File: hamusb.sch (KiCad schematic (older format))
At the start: 20 parts, among them P1 USB, P2 DATA, Q1 2N7002E, U1 FT232RL, U2 74AC125, Y1 12MHz

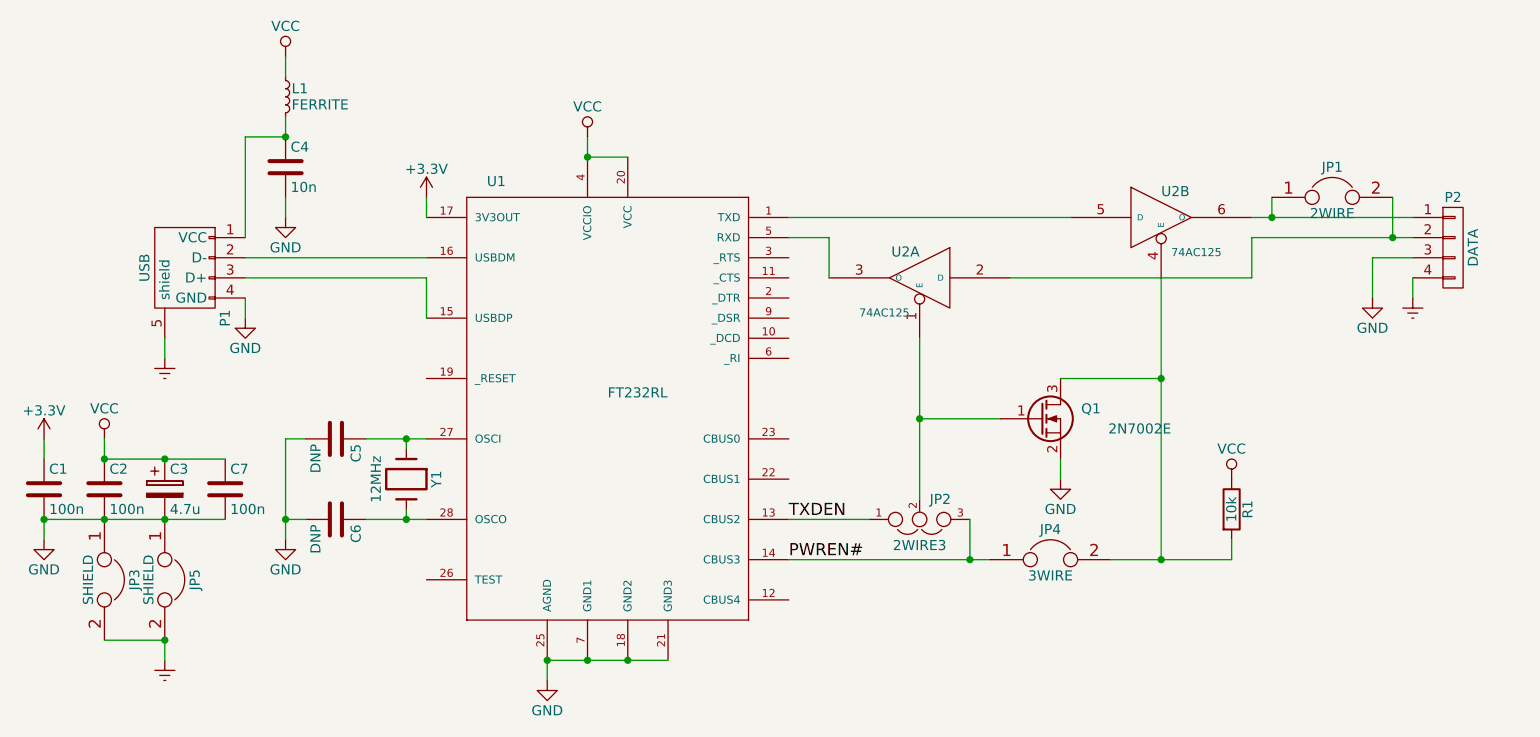
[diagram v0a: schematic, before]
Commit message: Cleanup, swapped logic gates, reordered input power circuit
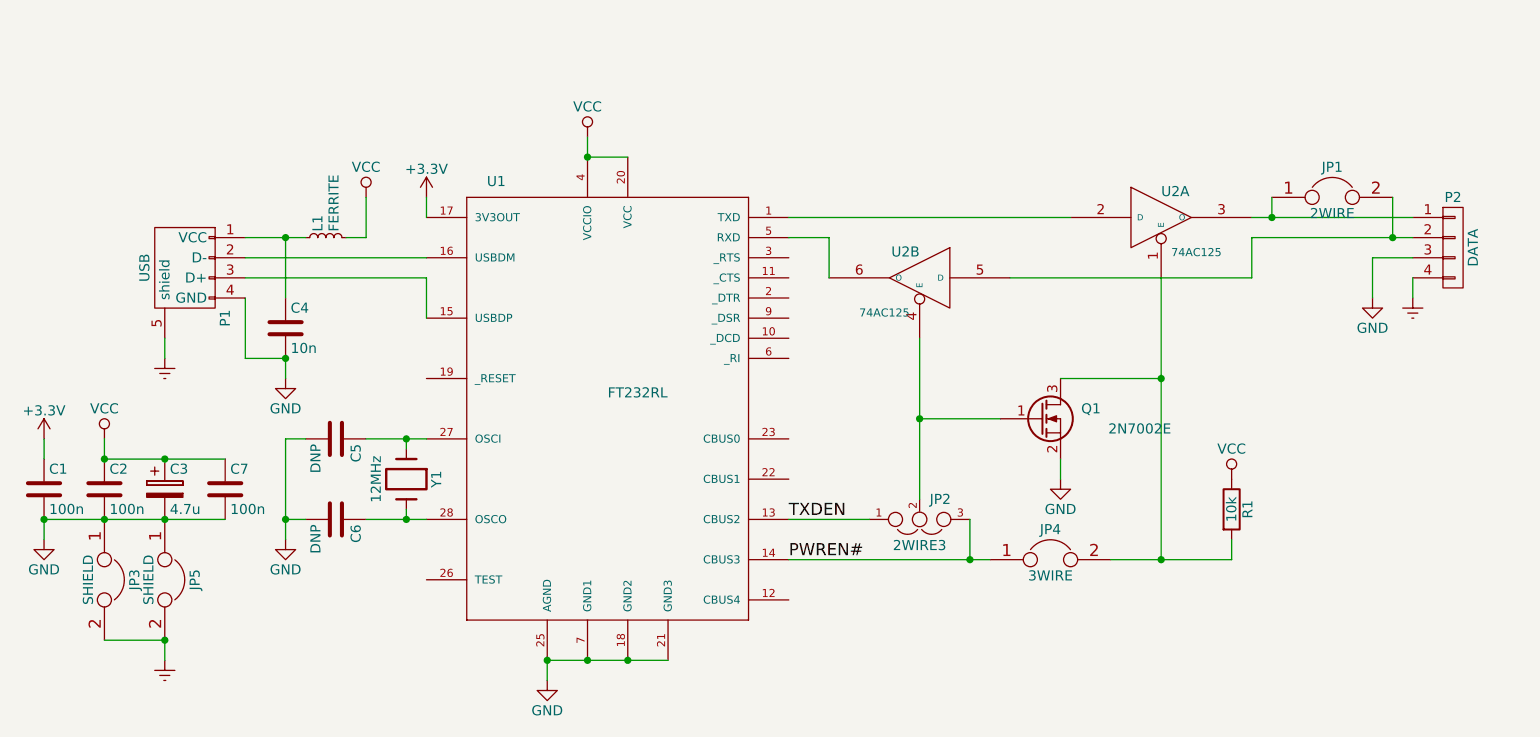
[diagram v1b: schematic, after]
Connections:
- net VCC: now also L1.2; no longer L1.1
- net at U1.1 (TXD): now also U2.2 (D); no longer U2.5 (D)
- net at U1.5 (RXD): now also U2.6 (O); no longer U2.3 (O)
- net at C4.1, P1.1 (VCC): now also L1.1; no longer L1.2
- net at JP1.1, P2.1 (P1): now also U2.3 (O); no longer U2.6 (O)
- net at JP1.2, P2.2 (P2): now also U2.5 (D); no longer U2.2 (D)
- net at JP4.2, Q1.3 (D), R1.2: now also U2.1 (E); no longer U2.4 (E)
- net at JP2.2, Q1.1 (G): now also U2.4 (E); no longer U2.1 (E)
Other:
- moved on the sheet: C4, L1
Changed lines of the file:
@@
 Sheet 1 1
 Title "Ham Radio USB Data Programmer"
-Date "2015-10-26"
-Rev "3"
+Date "2015-10-27"
+Rev "4"
 Comp "© 2015 Gregor Riepl"
 Comment1 "Licensed under the CERN OHL v1.2"
@@
 L C C4
 U 1 1 561BE2FB
-P 3900 2600
-F 0 "C4" H 3925 2700 50  0000 L CNN
-F 1 "10n" H 3925 2500 50  0000 L CNN
-F 2 "Capacitors_SMD:C_0805_HandSoldering" H 3938 2450 30  0001 C CNN
-F 3 "" H 3900 2600 60  0000 C CNN
-	1    3900 2600
+P 3900 3400
+F 0 "C4" H 3925 3500 50  0000 L CNN
+F 1 "10n" H 3925 3300 50  0000 L CNN
+F 2 "Capacitors_SMD:C_0805_HandSoldering" H 3938 3250 30  0001 C CNN
+F 3 "" H 3900 3400 60  0000 C CNN
+	1    3900 3400
 	1    0    0    -1
 $EndComp
@@
 L L_Small L1
 U 1 1 561BE3F0
-P 3900 2250
-F 0 "L1" H 3930 2290 50  0000 L CNN
-F 1 "FERRITE" H 3930 2210 50  0000 L CNN
-F 2 "Resistors_SMD:R_0805_HandSoldering" H 3900 2250 60  0001 C CNN
-F 3 "" H 3900 2250 60  0000 C CNN
-	1    3900 2250
-	1    0    0    -1
+P 4100 2950
+F 0 "L1" H 4130 2990 50  0000 L CNN
+F 1 "FERRITE" H 4130 2910 50  0000 L CNN
+F 2 "Resistors_SMD:R_0805_HandSoldering" H 4100 2950 60  0001 C CNN
+F 3 "" H 4100 2950 60  0000 C CNN
+	1    4100 2950
+	0    -1   -1   0
 $EndComp
 $Comp
@@
 L VCC #PWR07
 U 1 1 561BED9C
-P 3900 2050
-F 0 "#PWR07" H 3900 1900 50  0001 C CNN
-F 1 "VCC" H 3900 2200 50  0000 C CNN
-F 2 "" H 3900 2050 60  0000 C CNN
-F 3 "" H 3900 2050 60  0000 C CNN
-	1    3900 2050
-	1    0    0    -1
-$EndComp
-$Comp
-L GND #PWR08
-U 1 1 561BEE77
-P 3700 3350
-F 0 "#PWR08" H 3700 3100 50  0001 C CNN
-F 1 "GND" H 3700 3200 50  0000 C CNN
-F 2 "" H 3700 3350 60  0000 C CNN
-F 3 "" H 3700 3350 60  0000 C CNN
-	1    3700 3350
-	1    0    0    -1
-$EndComp
-Wire Wire Line
-	3700 3250 3700 3350
-$Comp
-L Earth #PWR09
+P 4300 2750
+F 0 "#PWR07" H 4300 2600 50  0001 C CNN
+F 1 "VCC" H 4300 2900 50  0000 C CNN
+F 2 "" H 4300 2750 60  0000 C CNN
+F 3 "" H 4300 2750 60  0000 C CNN
+	1    4300 2750
+	1    0    0    -1
+$EndComp
+Wire Wire Line
+	3700 3250 3700 3550
+$Comp
+L Earth #PWR08
 U 1 1 561BEEB0
 P 3300 3550
-F 0 "#PWR09" H 3300 3300 50  0001 C CNN
+F 0 "#PWR08" H 3300 3300 50  0001 C CNN
 F 1 "Earth" H 3300 3400 50  0001 C CNN
 F 2 "" H 3300 3550 60  0000 C CNN
@@
 Wire Wire Line
 	3000 4350 3000 4350
-Wire Wire Line
-	3700 2950 3700 2450
-Connection ~ 3900 2450
-$Comp
-L GND #PWR010
+$Comp
+L GND #PWR09
 U 1 1 561BF7EA
-P 3900 2850
-F 0 "#PWR010" H 3900 2600 50  0001 C CNN
-F 1 "GND" H 3900 2700 50  0000 C CNN
-F 2 "" H 3900 2850 60  0000 C CNN
-F 3 "" H 3900 2850 60  0000 C CNN
-	1    3900 2850
-	1    0    0    -1
-$EndComp
-Wire Wire Line
-	3900 2850 3900 2750
+P 3900 3650
+F 0 "#PWR09" H 3900 3400 50  0001 C CNN
+F 1 "GND" H 3900 3500 50  0000 C CNN
+F 2 "" H 3900 3650 60  0000 C CNN
+F 3 "" H 3900 3650 60  0000 C CNN
+	1    3900 3650
+	1    0    0    -1
+$EndComp
+Wire Wire Line
+	3900 3650 3900 3550
 Wire Wire Line
 	3700 3150 4600 3150
@@
 Connection ~ 9400 2950
 $Comp
-L GND #PWR011
+L GND #PWR010
 U 1 1 561C060F
 P 9300 3250
-F 0 "#PWR011" H 9300 3000 50  0001 C CNN
+F 0 "#PWR010" H 9300 3000 50  0001 C CNN
 F 1 "GND" H 9300 3100 50  0000 C CNN
 F 2 "" H 9300 3250 60  0000 C CNN
@@
 $EndComp
 $Comp
-L Earth #PWR012
+L Earth #PWR011
 U 1 1 561C0615
 P 9500 3250
-F 0 "#PWR012" H 9500 3000 50  0001 C CNN
+F 0 "#PWR011" H 9500 3000 50  0001 C CNN
 F 1 "Earth" H 9500 3100 50  0001 C CNN
 F 2 "" H 9500 3250 60  0000 C CNN
@@
 Connection ~ 4500 4350
 $Comp
-L GND #PWR013
+L GND #PWR012
 U 1 1 561C13F7
 P 3900 4450
-F 0 "#PWR013" H 3900 4200 50  0001 C CNN
+F 0 "#PWR012" H 3900 4200 50  0001 C CNN
 F 1 "GND" H 3900 4300 50  0000 C CNN
 F 2 "" H 3900 4450 60  0000 C CNN
@@
 $EndComp
 $Comp
-L VCC #PWR014
+L VCC #PWR013
 U 1 1 561C2002
 P 8600 4150
-F 0 "#PWR014" H 8600 4000 50  0001 C CNN
+F 0 "#PWR013" H 8600 4000 50  0001 C CNN
 F 1 "VCC" H 8600 4300 50  0000 C CNN
 F 2 "" H 8600 4150 60  0000 C CNN
@@
 $Comp
 L 74LS125 U2
-U 2 1 561D1FD3
+U 1 1 561D1FD3
 P 8250 2850
 F 0 "U2" H 8250 2950 50  0000 L BNN
@@
 F 2 "Housings_SSOP:TSSOP-14_4.4x5mm_Pitch0.65mm" H 8250 2850 60  0001 C CNN
 F 3 "" H 8250 2850 60  0000 C CNN
-	2    8250 2850
+	1    8250 2850
 	1    0    0    -1
 $EndComp
 $Comp
 L 74LS125 U2
-U 1 1 561D22A1
+U 2 1 561D22A1
 P 7050 3150
 F 0 "U2" H 7050 3250 50  0000 L BNN
@@
 F 2 "Housings_SSOP:TSSOP-14_4.4x5mm_Pitch0.65mm" H 7050 3150 60  0001 C CNN
 F 3 "" H 7050 3150 60  0000 C CNN
-	1    7050 3150
+	2    7050 3150
 	-1   0    0    -1
 $EndComp
@@
 $EndComp
 $Comp
-L GND #PWR015
+L GND #PWR014
 U 1 1 561F1B86
 P 7750 4150
-F 0 "#PWR015" H 7750 3900 50  0001 C CNN
+F 0 "#PWR014" H 7750 3900 50  0001 C CNN
 F 1 "GND" H 7750 4000 50  0000 C CNN
 F 2 "" H 7750 4150 60  0000 C CNN
@@
 Connection ~ 7050 3850
 $Comp
-L Earth #PWR016
+L Earth #PWR015
 U 1 1 56202936
 P 3300 5050
-F 0 "#PWR016" H 3300 4800 50  0001 C CNN
+F 0 "#PWR015" H 3300 4800 50  0001 C CNN
 F 1 "Earth" H 3300 4900 50  0001 C CNN
 F 2 "" H 3300 5050 60  0000 C CNN
@@
 	3300 4950 3000 4950
 Wire Wire Line
-	3700 2450 3900 2450
-Wire Wire Line
-	3900 2450 3900 2350
-Wire Wire Line
-	3900 2150 3900 2050
+	3700 2950 4000 2950
+Wire Wire Line
+	3900 2950 3900 3250
+Connection ~ 3900 2950
+Wire Wire Line
+	4200 2950 4300 2950
+Wire Wire Line
+	4300 2950 4300 2750
+Wire Wire Line
+	3900 3550 3700 3550
+Connection ~ 3900 3550
 $EndSCHEMATC

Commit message: Added additional net labels Increased shield copper area
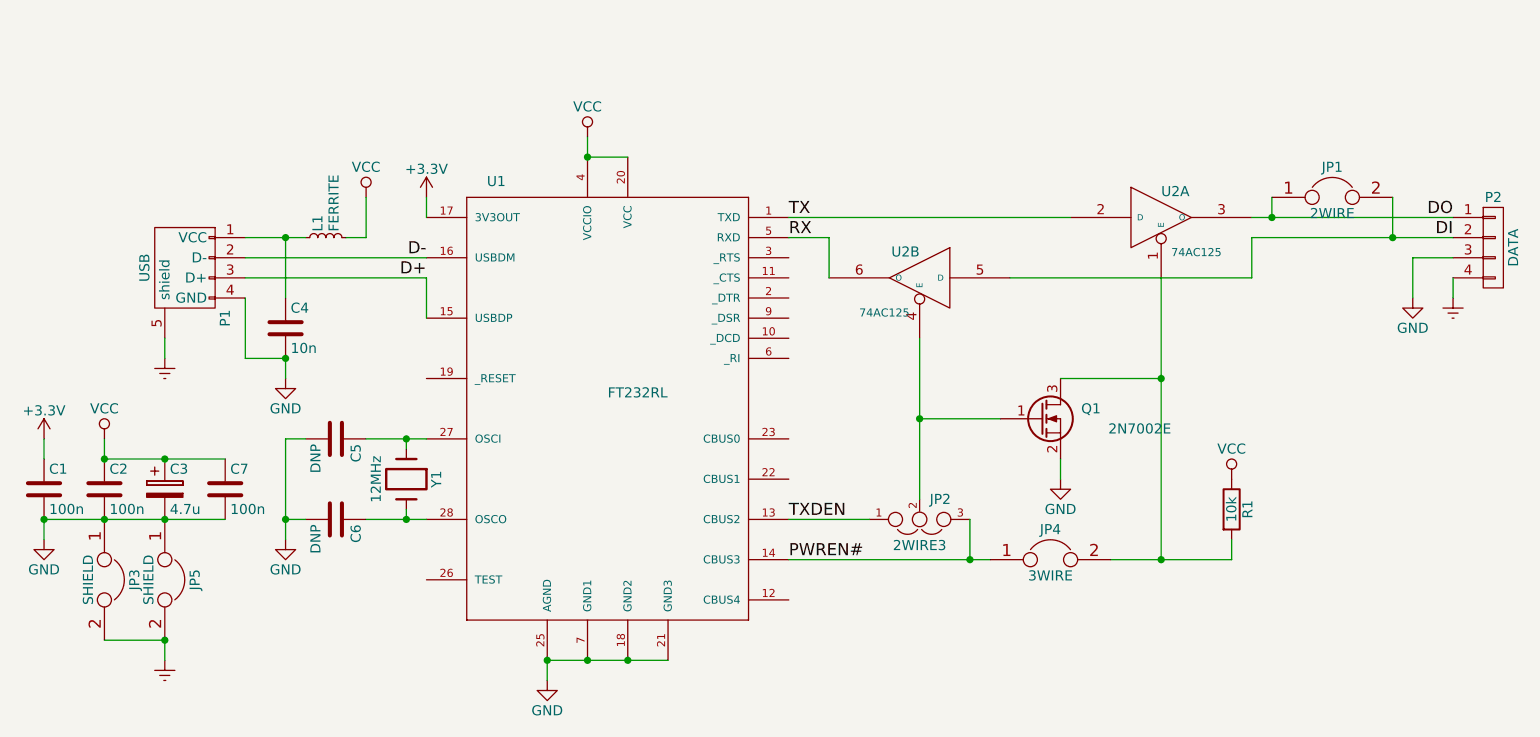
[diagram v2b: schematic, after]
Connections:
- net TX: now reaches U1.1 (TXD), U2.2 (D)
- net D+: now reaches P1.3 (D+), U1.15 (USBDP)
- net D-: now reaches P1.2 (D-), U1.16 (USBDM)
- net RX: now reaches U1.5 (RXD), U2.6 (O)
- net DO: now reaches JP1.1, P2.1 (P1), U2.3 (O)
- net DI: now reaches JP1.2, P2.2 (P2), U2.5 (D)
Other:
- moved on the sheet: P2
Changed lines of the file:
@@
 Title "Ham Radio USB Data Programmer"
 Date "2015-10-27"
-Rev "4"
+Rev "5"
 Comp "© 2015 Gregor Riepl"
 Comment1 "Licensed under the CERN OHL v1.2"
@@
 L CONN_01X04 P2
 U 1 1 561C0067
-P 9700 3000
-F 0 "P2" H 9700 3250 50  0000 C CNN
-F 1 "DATA" V 9800 3000 50  0000 C CNN
-F 2 "Pin_Headers:Pin_Header_Straight_1x04" H 9700 3000 60  0001 C CNN
-F 3 "" H 9700 3000 60  0000 C CNN
-	1    9700 3000
-	1    0    0    -1
-$EndComp
-Wire Wire Line
-	8700 2850 9500 2850
+P 9900 3000
+F 0 "P2" H 9900 3250 50  0000 C CNN
+F 1 "DATA" V 10000 3000 50  0000 C CNN
+F 2 "Pin_Headers:Pin_Header_Straight_1x04" H 9900 3000 60  0001 C CNN
+F 3 "" H 9900 3000 60  0000 C CNN
+	1    9900 3000
+	1    0    0    -1
+$EndComp
+Wire Wire Line
+	8700 2850 9700 2850
 Wire Wire Line
 	8800 2850 8800 2750
 Wire Wire Line
-	8700 2950 9500 2950
+	8700 2950 9700 2950
 Wire Wire Line
 	9400 2950 9400 2750
@@
 L GND #PWR010
 U 1 1 561C060F
-P 9300 3250
-F 0 "#PWR010" H 9300 3000 50  0001 C CNN
-F 1 "GND" H 9300 3100 50  0000 C CNN
-F 2 "" H 9300 3250 60  0000 C CNN
-F 3 "" H 9300 3250 60  0000 C CNN
-	1    9300 3250
-	1    0    0    -1
-$EndComp
-$Comp
-L Earth #PWR011
-U 1 1 561C0615
 P 9500 3250
-F 0 "#PWR011" H 9500 3000 50  0001 C CNN
-F 1 "Earth" H 9500 3100 50  0001 C CNN
+F 0 "#PWR010" H 9500 3000 50  0001 C CNN
+F 1 "GND" H 9500 3100 50  0000 C CNN
 F 2 "" H 9500 3250 60  0000 C CNN
 F 3 "" H 9500 3250 60  0000 C CNN
@@
 	1    0    0    -1
 $EndComp
-Wire Wire Line
-	9500 3050 9300 3050
-Wire Wire Line
-	9300 3050 9300 3250
-Wire Wire Line
-	9500 3150 9500 3250
+$Comp
+L Earth #PWR011
+U 1 1 561C0615
+P 9700 3250
+F 0 "#PWR011" H 9700 3000 50  0001 C CNN
+F 1 "Earth" H 9700 3100 50  0001 C CNN
+F 2 "" H 9700 3250 60  0000 C CNN
+F 3 "" H 9700 3250 60  0000 C CNN
+	1    9700 3250
+	1    0    0    -1
+$EndComp
+Wire Wire Line
+	9700 3050 9500 3050
+Wire Wire Line
+	9500 3050 9500 3250
+Wire Wire Line
+	9700 3150 9700 3250
 $Comp
 L Crystal Y1
@@
 	3900 3550 3700 3550
 Connection ~ 3900 3550
+Text Label 6400 2850 0    60   ~ 0
+TX
+Text Label 6400 2950 0    60   ~ 0
+RX
+Text Label 9700 2950 2    60   ~ 0
+DI
+Text Label 9700 2850 2    60   ~ 0
+DO
+Text Label 4600 3150 2    60   ~ 0
+D+
+Text Label 4600 3050 2    60   ~ 0
+D-
 $EndSCHEMATC
